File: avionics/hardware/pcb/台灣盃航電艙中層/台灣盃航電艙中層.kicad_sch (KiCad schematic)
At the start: 68 parts, among them J2 Micro_SD_Card_Det2, J3 Conn_01x04_Pin, J4 Pyro1, J5 Pyro2, Q1 NMOS, Q2 NMOS, SW1 SW_Nidec_CAS-120A1, U1 STM32F405VGT6, U2 BMI088, U3 BMP390L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

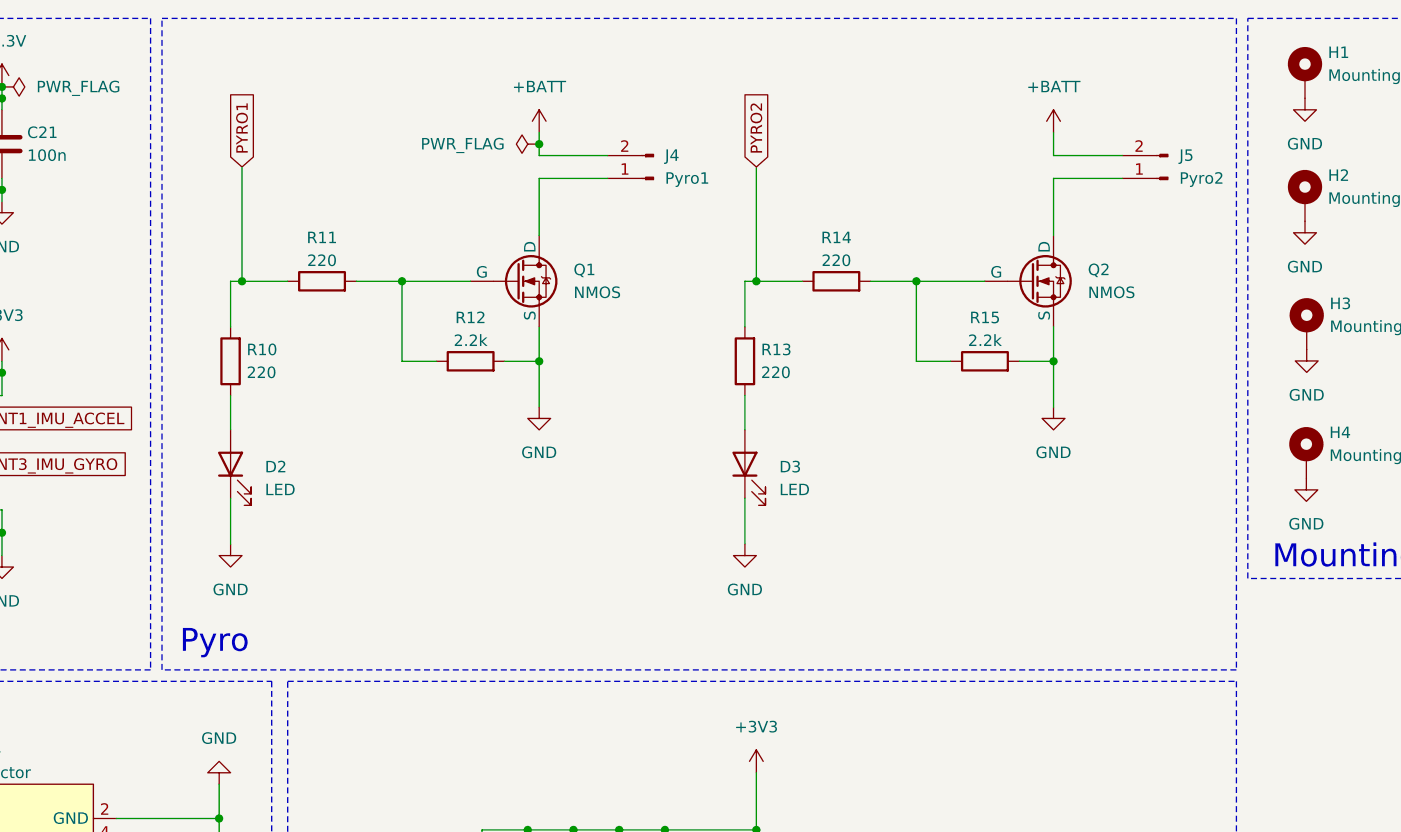
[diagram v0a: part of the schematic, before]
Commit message: 更新下層PCB原理圖
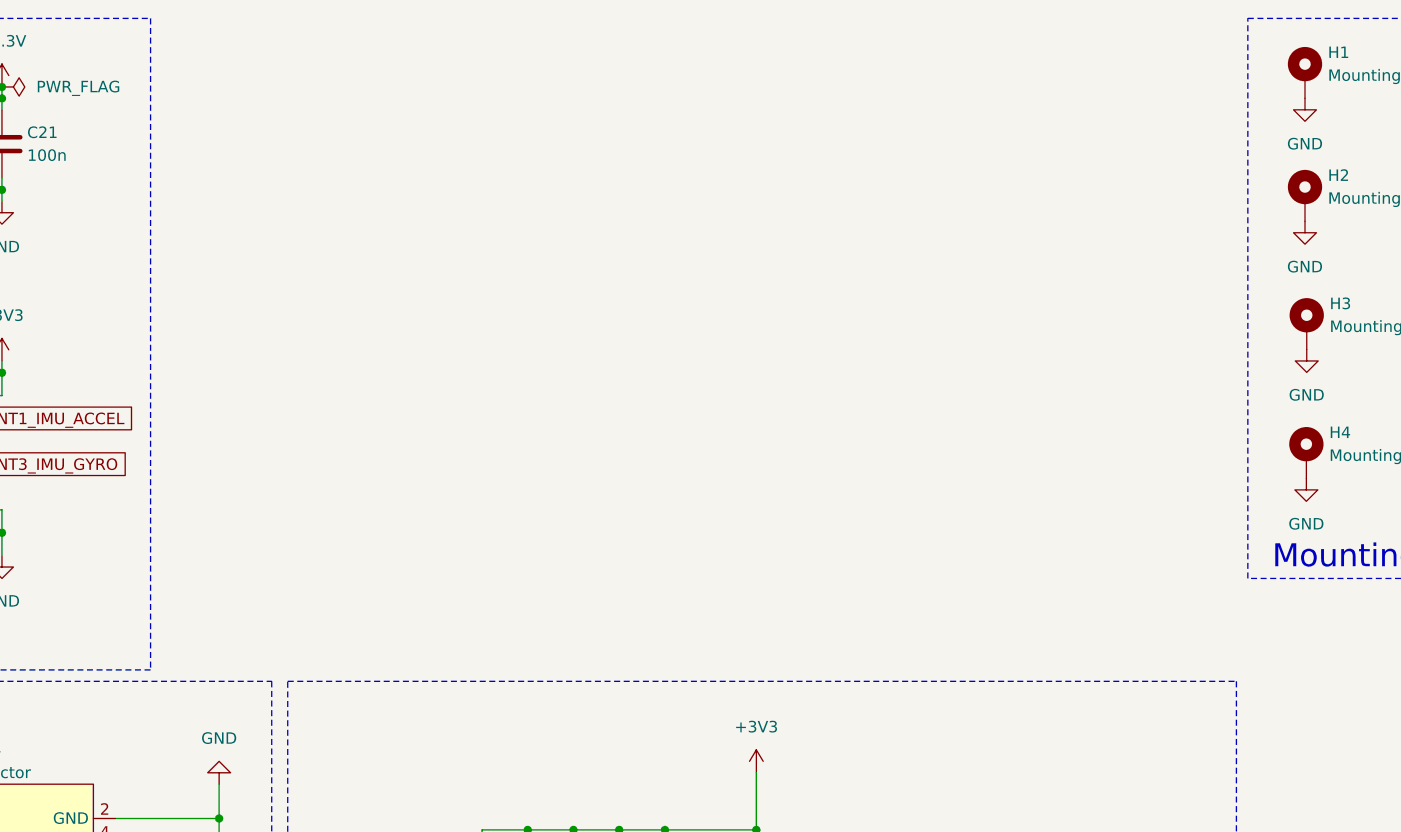
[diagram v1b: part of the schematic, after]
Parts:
- removed D2, D3: LED, LED_SMD:LED_0805_2012Metric, symbol Device:LED
- removed J4: Pyro1, Connector_JST:JST_XH_B2B-XH-A_1x02_P2.50mm_Vertical, symbol Connector:Conn_01x02_Pin
- removed J5: Pyro2, Connector_JST:JST_XH_B2B-XH-A_1x02_P2.50mm_Vertical, symbol Connector:Conn_01x02_Pin
- removed Q1, Q2: NMOS, Package_TO_SOT_SMD:SOT-223, symbol Simulation_SPICE:NMOS
- removed R10, R11, R13, R14: 220, Resistor_SMD:R_0805_2012Metric, symbol Device:R
- removed R12, R15: 2.2k, Resistor_SMD:R_0805_2012Metric, symbol Device:R
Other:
- note removed: "Pyro"

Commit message: V1.0板
更新原理圖
layout 完PCB，並且沒有任何DRC錯誤及警告
增加三個感測器的封裝上去
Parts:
- removed C30: 47u, Capacitor_SMD:C_0805_2012Metric, symbol Device:C
- removed C31: 100n, Capacitor_SMD:C_0603_1608Metric, symbol Device:C
- removed SW1: SW_Nidec_CAS-120A1, Button_Switch_SMD:Nidec_Copal_CAS-120A, symbol Switch:SW_Nidec_CAS-120A1
- added SW1: SW_SPST, Button_Switch_SMD:SW_SPST_FSMSM, symbol Switch:SW_SPST
- H1, H2, H3, H4: footprint (none) -> MountingHole:MountingHole_3.2mm_M3_ISO14580_Pad
- U3: footprint BMP390L:XDCR_BMP390L -> Bmp390l:XDCR_BMP390L
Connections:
- net +3.3V is gone; now on net +3V3: C17.1, C19.1, C20.1, C21.1
- net +3V3: no longer U4.31 (3V3)
- net GND: now also SW1.1 (A)
- net at C5.1, R2.2, U1.14 (NRST): now also SW1.2 (B)
- net +BATT: no longer names the net of U4.33 (BATT)
- no-connect marks 36 -> 38
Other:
- moved on the sheet: H1, H2, H3, H4
